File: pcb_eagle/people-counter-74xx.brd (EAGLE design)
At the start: 70 x 69 mm, 76 parts, among them IC1 74LS90N, IC2 74LS90N, IC3 74LS90N, IC4 74LS90N, IC5 74LS47N, IC6 74LS47N, IC7 74LS47N, IC8 74LS47N, IC9 NE555N, X1 USB-MICRO-B-BOTTOM

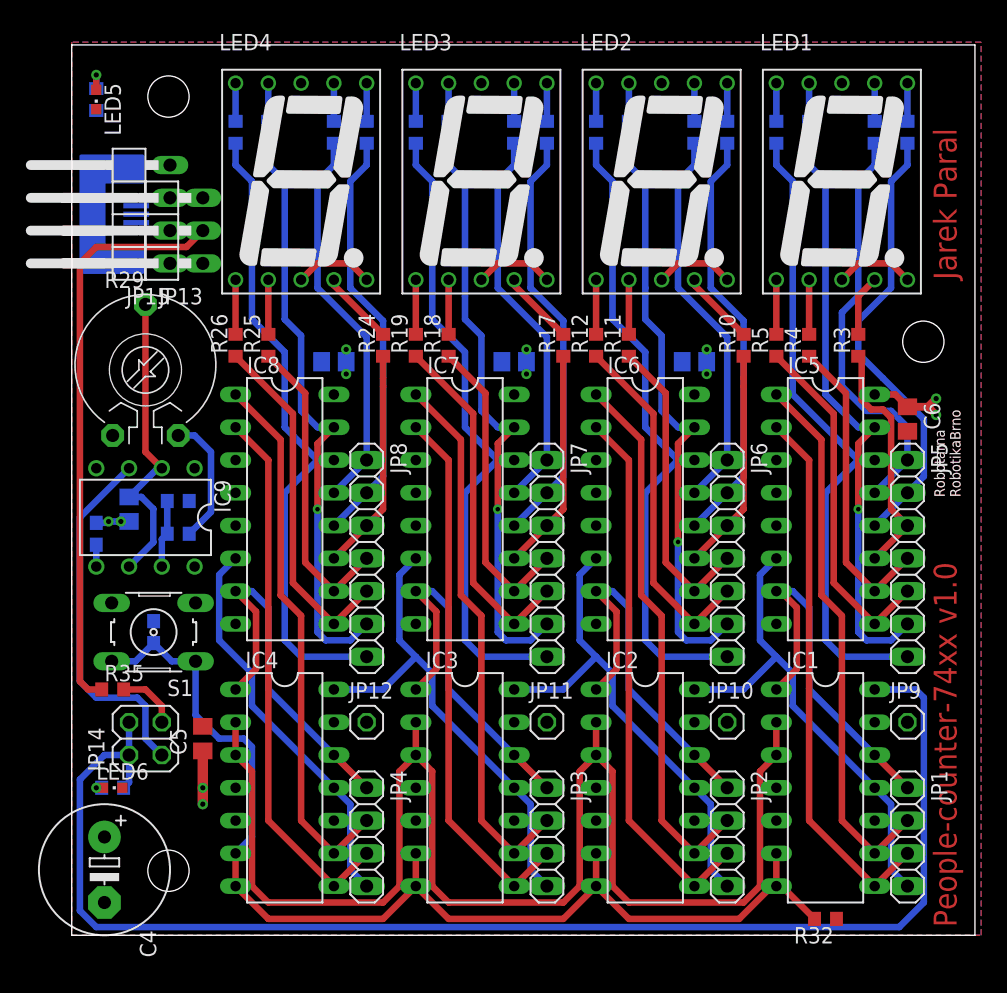
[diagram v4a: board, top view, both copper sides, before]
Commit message: PCB_EAGLE: start work on version 1.1 - repair layer of texts Robotarna RobotikaBrno
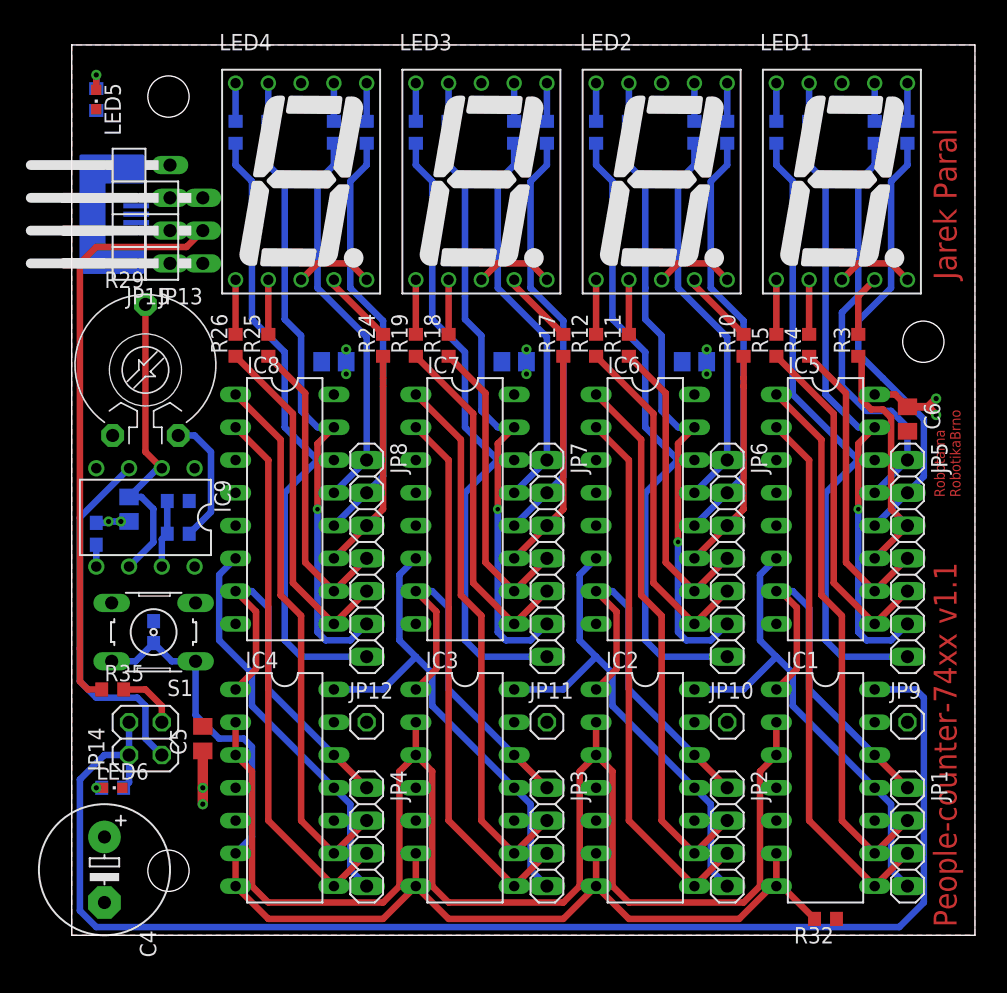
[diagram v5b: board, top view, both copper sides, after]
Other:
- board text added: "People-counter-74xx v1.1"
- board text removed: "People-counter-74xx v1.0"
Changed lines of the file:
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@@
 <setting verticaltext="up"/>
 </settings>
-<grid distance="0.025" unitdist="inch" unit="inch" style="lines" multiple="1" display="yes" altdistance="0.0125" altunitdist="inch" altunit="inch"/>
+<grid distance="0.025" unitdist="inch" unit="mm" style="lines" multiple="1" display="yes" altdistance="0.0125" altunitdist="inch" altunit="inch"/>
 <layers>
 <layer number="1" name="Top" color="4" fill="1" visible="yes" active="yes"/>
@@
 <layer number="21" name="tPlace" color="7" fill="1" visible="yes" active="yes"/>
 <layer number="22" name="bPlace" color="7" fill="1" visible="yes" active="yes"/>
-<layer number="23" name="tOrigins" color="15" fill="1" visible="yes" active="yes"/>
-<layer number="24" name="bOrigins" color="15" fill="1" visible="yes" active="yes"/>
-<layer number="25" name="tNames" color="7" fill="1" visible="yes" active="yes"/>
-<layer number="26" name="bNames" color="7" fill="1" visible="yes" active="yes"/>
-<layer number="27" name="tValues" color="7" fill="1" visible="yes" active="yes"/>
-<layer number="28" name="bValues" color="7" fill="1" visible="yes" active="yes"/>
+<layer number="23" name="tOrigins" color="15" fill="1" visible="no" active="yes"/>
+<layer number="24" name="bOrigins" color="15" fill="1" visible="no" active="yes"/>
+<layer number="25" name="tNames" color="7" fill="1" visible="no" active="yes"/>
+<layer number="26" name="bNames" color="7" fill="1" visible="no" active="yes"/>
+<layer number="27" name="tValues" color="7" fill="1" visible="no" active="yes"/>
+<layer number="28" name="bValues" color="7" fill="1" visible="no" active="yes"/>
 <layer number="29" name="tStop" color="7" fill="3" visible="no" active="yes"/>
 <layer number="30" name="bStop" color="7" fill="6" visible="no" active="yes"/>
@@
 <text x="64.135" y="13.335" size="1.778" layer="51" font="vector" ratio="20">1</text>
 <text x="64.135" y="0.635" size="1.778" layer="51" font="vector" ratio="20">8</text>
-<text x="50.165" y="38.735" size="1.778" layer="51" font="vector" ratio="20">A</text>
-<text x="50.165" y="18.415" size="1.778" layer="51" font="vector" ratio="20">G</text>
-<text x="50.165" y="13.335" size="1.778" layer="51" font="vector" ratio="20">1</text>
-<text x="50.165" y="0.635" size="1.778" layer="51" font="vector" ratio="20">8</text>
-<text x="36.195" y="38.735" size="1.778" layer="51" font="vector" ratio="20">A</text>
-<text x="36.195" y="18.415" size="1.778" layer="51" font="vector" ratio="20">G</text>
-<text x="36.195" y="13.335" size="1.778" layer="51" font="vector" ratio="20">1</text>
-<text x="36.195" y="0.635" size="1.778" layer="51" font="vector" ratio="20">8</text>
-<text x="22.225" y="38.735" size="1.778" layer="51" font="vector" ratio="20">A</text>
-<text x="22.225" y="18.415" size="1.778" layer="51" font="vector" ratio="20">G</text>
-<text x="22.225" y="13.335" size="1.778" layer="51" font="vector" ratio="20">1</text>
+<text x="52.07" y="38.735" size="1.778" layer="51" font="vector" ratio="20">A</text>
+<text x="52.3875" y="18.415" size="1.778" layer="51" font="vector" ratio="20">G</text>
+<text x="52.3875" y="13.335" size="1.778" layer="51" font="vector" ratio="20">1</text>
+<text x="52.3875" y="0.635" size="1.778" layer="51" font="vector" ratio="20">8</text>
+<text x="38.1" y="38.735" size="1.778" layer="51" font="vector" ratio="20">A</text>
+<text x="38.4175" y="18.415" size="1.778" layer="51" font="vector" ratio="20">G</text>
+<text x="38.4175" y="13.335" size="1.778" layer="51" font="vector" ratio="20">1</text>
+<text x="38.4175" y="0.635" size="1.778" layer="51" font="vector" ratio="20">8</text>
+<text x="24.13" y="38.735" size="1.778" layer="51" font="vector" ratio="20">A</text>
+<text x="24.4475" y="18.415" size="1.778" layer="51" font="vector" ratio="20">G</text>
+<text x="24.4475" y="13.335" size="1.778" layer="51" font="vector" ratio="20">1</text>
 <hole x="66" y="46" drill="3.2"/>
 <hole x="7.5" y="65" drill="3.2"/>
 <hole x="7.5" y="5" drill="3.2"/>
 <circle x="7.5" y="65" radius="3" width="0.508" layer="51"/>
-<circle x="7.5" y="5" radius="3" width="0.508" layer="52"/>
+<circle x="7.5" y="5" radius="3" width="0.508" layer="51"/>
 <circle x="66" y="46" radius="3" width="0.508" layer="51"/>
-<text x="68.58" y="0.635" size="1.778" layer="1" font="vector" ratio="20" rot="R90">People-counter-74xx v1.0</text>
+<text x="68.58" y="0.635" size="1.778" layer="1" font="vector" ratio="20" rot="R90">People-counter-74xx v1.1</text>
 <text x="68.58" y="50.8" size="1.778" layer="1" font="vector" ratio="20" rot="R90">Jarek Paral</text>
 <text x="68.58" y="50.8" size="1.778" layer="51" font="vector" ratio="20" rot="R90">Jarek Paral</text>
-<text x="68.58" y="0.635" size="1.778" layer="51" font="vector" ratio="20" rot="R90">People-counter-74xx v1.0</text>
-<text x="68.8835" y="33.954" size="0.8128" layer="21" font="vector" ratio="20" rot="R90">Robotarna
+<text x="68.58" y="0.635" size="1.778" layer="51" font="vector" ratio="20" rot="R90">People-counter-74xx v1.1</text>
+<text x="68.8835" y="33.954" size="0.8128" layer="51" font="vector" ratio="20" rot="R90">Robotarna
 RobotikaBrno</text>
 <text x="68.8835" y="33.954" size="0.8128" layer="1" font="vector" ratio="20" rot="R90">Robotarna
@@
 <contactref element="IC5" pad="8"/>
 <polygon width="0.1524" layer="1">
-<vertex x="0" y="69.215"/>
+<vertex x="0" y="69"/>
 <vertex x="0" y="0"/>
-<vertex x="70.485" y="0"/>
-<vertex x="70.485" y="69.215"/>
+<vertex x="70" y="0"/>
+<vertex x="70" y="69"/>
 </polygon>
 <contactref element="JP9" pad="1"/>
@@
 <contactref element="IC5" pad="5"/>
 <polygon width="0.1524" layer="16">
-<vertex x="0" y="69.215"/>
+<vertex x="0" y="69"/>
 <vertex x="0" y="0"/>
-<vertex x="70.485" y="0"/>
-<vertex x="70.485" y="69.215"/>
+<vertex x="70" y="0"/>
+<vertex x="70" y="69"/>
 </polygon>
 <contactref element="IC2" pad="5"/>

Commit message: PCB_EAGLE: fix two bugs from v1.0 - change value of C2 (10u -> 200n) - delete one wire on potentiometer (R29)
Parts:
- C2: value 10u -> 200n
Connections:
- net GND: no longer R29.1
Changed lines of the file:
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@@
 <?xml version="1.0" encoding="utf-8"?>
 <!DOCTYPE eagle SYSTEM "eagle.dtd">
-<eagle version="8.6.0">
+<eagle version="9.1.2">
 <drawing>
 <settings>
@@
 <layer number="21" name="tPlace" color="7" fill="1" visible="yes" active="yes"/>
 <layer number="22" name="bPlace" color="7" fill="1" visible="yes" active="yes"/>
-<layer number="23" name="tOrigins" color="15" fill="1" visible="no" active="yes"/>
-<layer number="24" name="bOrigins" color="15" fill="1" visible="no" active="yes"/>
+<layer number="23" name="tOrigins" color="15" fill="1" visible="yes" active="yes"/>
+<layer number="24" name="bOrigins" color="15" fill="1" visible="yes" active="yes"/>
 <layer number="25" name="tNames" color="7" fill="1" visible="no" active="yes"/>
 <layer number="26" name="bNames" color="7" fill="1" visible="no" active="yes"/>
@@
 <param name="checkStop" value="0"/>
 <param name="checkValues" value="0"/>
+<param name="checkNames" value="1"/>
+<param name="checkWireStubs" value="1"/>
+<param name="checkPolygonWidth" value="0"/>
 <param name="useDiameter" value="13"/>
 <param name="maxErrors" value="50"/>
@@
 <attribute name="SPICEPREFIX" value="R" x="58.42" y="1.27" size="1.778" layer="27" rot="R180" display="off"/>
 </element>
-<element name="C2" library="rcl" library_urn="urn:adsk.eagle:library:334" package="C0805" package3d_urn="urn:adsk.eagle:package:23617/2" value="10u" x="4.445" y="33.02" rot="MR270">
+<element name="C2" library="rcl" library_urn="urn:adsk.eagle:library:334" package="C0805" package3d_urn="urn:adsk.eagle:package:23617/2" value="200n" x="4.445" y="33.02" rot="MR270">
 <attribute name="SPICEPREFIX" value="C" x="4.445" y="33.02" size="1.778" layer="28" rot="MR270" display="off"/>
 </element>
@@
 <contactref element="IC9" pad="1"/>
 <contactref element="C1" pad="1"/>
-<contactref element="R29" pad="1"/>
 <contactref element="IC3" pad="3"/>
 <contactref element="IC3" pad="2"/>
@@
 </signal>
 </signals>
+<mfgpreviewcolors>
+<mfgpreviewcolor name="soldermaskcolor" color="0xC8008000"/>
+<mfgpreviewcolor name="silkscreencolor" color="0xFFFEFEFE"/>
+<mfgpreviewcolor name="backgroundcolor" color="0xFF282828"/>
+<mfgpreviewcolor name="coppercolor" color="0xFFFFBF00"/>
+<mfgpreviewcolor name="substratecolor" color="0xFF786E46"/>
+</mfgpreviewcolors>
 </board>
 </drawing>
